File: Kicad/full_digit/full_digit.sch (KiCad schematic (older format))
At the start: 40 parts, among them J1 CONN_8, J2 CONN_8, J3 CONN_8, J4 CONN_8, J5 CONN_8, J6 CONN_8, J7 CONN_8, J8 CONN_8, U1 TLC5917, X1 MTHOLE, X2 MTHOLE, X3 MTHOLE, X4 MTHOLE

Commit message: Added new connectors to schematics
Added DNS connectors for Spark Core/Photon/Electron, Arduino
Uno/Micro/Nano. Also redacted access token for the Spark Core used for
the prototype clock. That Spark has been destroyed, so don't bother
trying to use the token.
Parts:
- removed PTC1, PTC2: 0ZCF0300AF2C, ~, symbol PTC
- added J10, J9: CONN_01X03, symbol CONN_01X03
- added J11, J12: CONN_01X12, symbol CONN_01X12
- added J13, J16: CONN_01X08, symbol CONN_01X08
- added J14: CONN_01X06, symbol CONN_01X06
- added J15: CONN_01X10, symbol CONN_01X10
- added J17, J18: CONN_01X17, symbol CONN_01X17
- added J19: RASM722X, symbol BARREL_JACK
- C2: value 4.7uF 25V -> 4.7uF 50V
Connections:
- net labels added: +5V, Vled
- net labels removed: VLED
- wire segments 81 -> 137
- no-connect marks 0 -> 59
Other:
- note added: "Arduino Micro/Nano Pro"
- note added: "Arduino Uno"
- note added: "Power Input"
- note added: "Regulator"
- note added: "Spark"
- note added: "Vled must be less than 20 V. \nVcc can be between 3.0 and 5.5 V. \nComms should match Vcc."
- note removed: "Vcc can be between 3.0 and 5.5 V. \nComms should match Vcc."
- moved on the sheet: C1, C2, D1, D10, D11, D12, D13, D14, D15, D16, D17, D18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

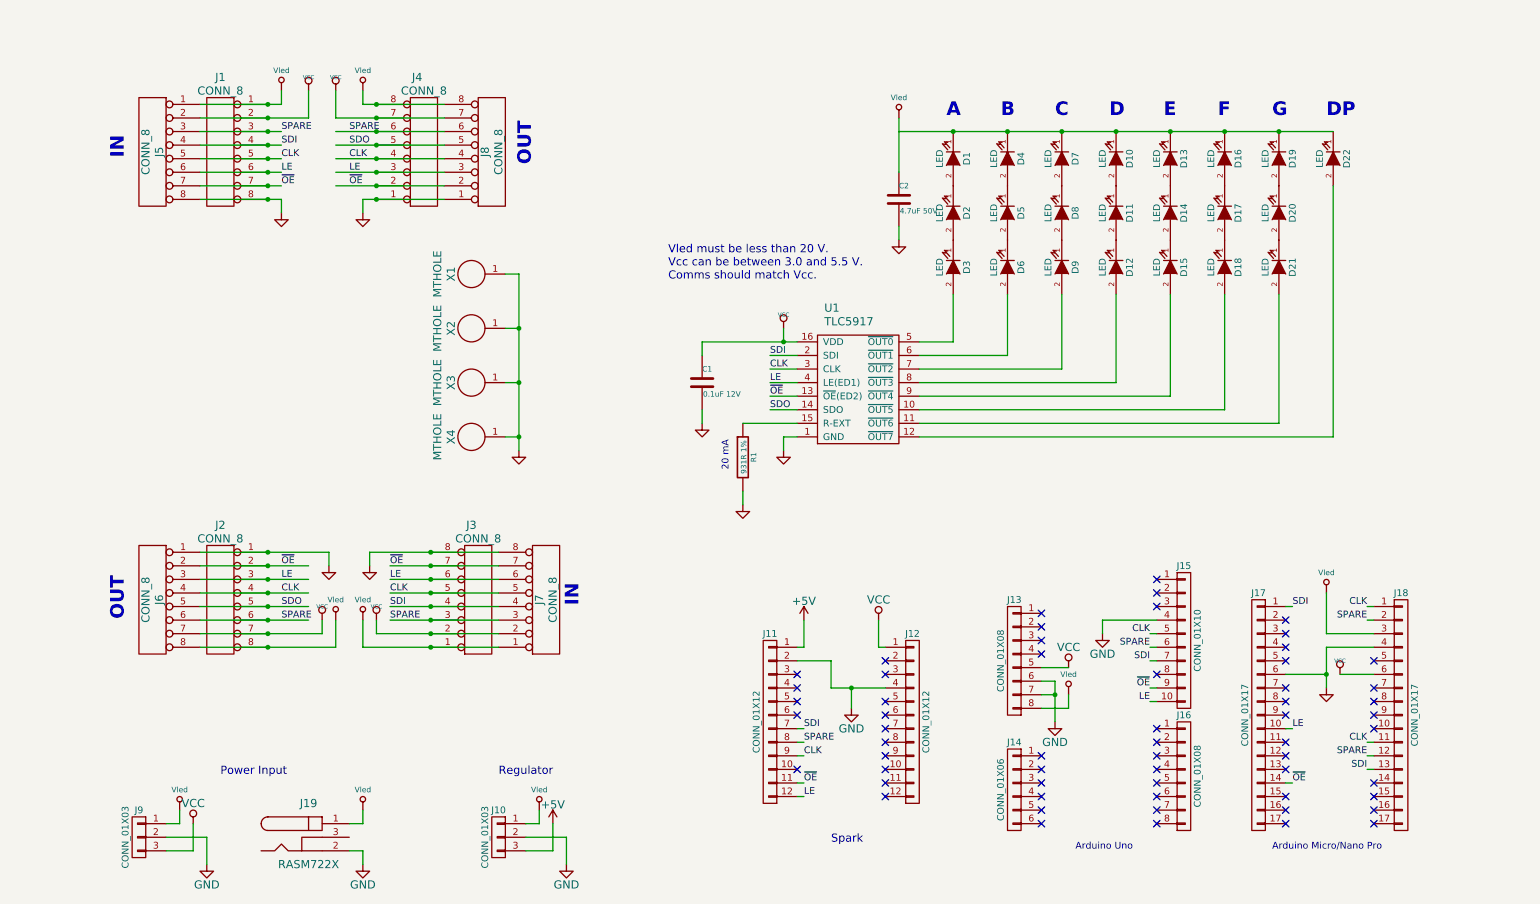
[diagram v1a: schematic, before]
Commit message: Placement of Rev 3
Placed new parts: Spark, Arduino Uno, Arduino Micro, and logo. Routing
still to do.
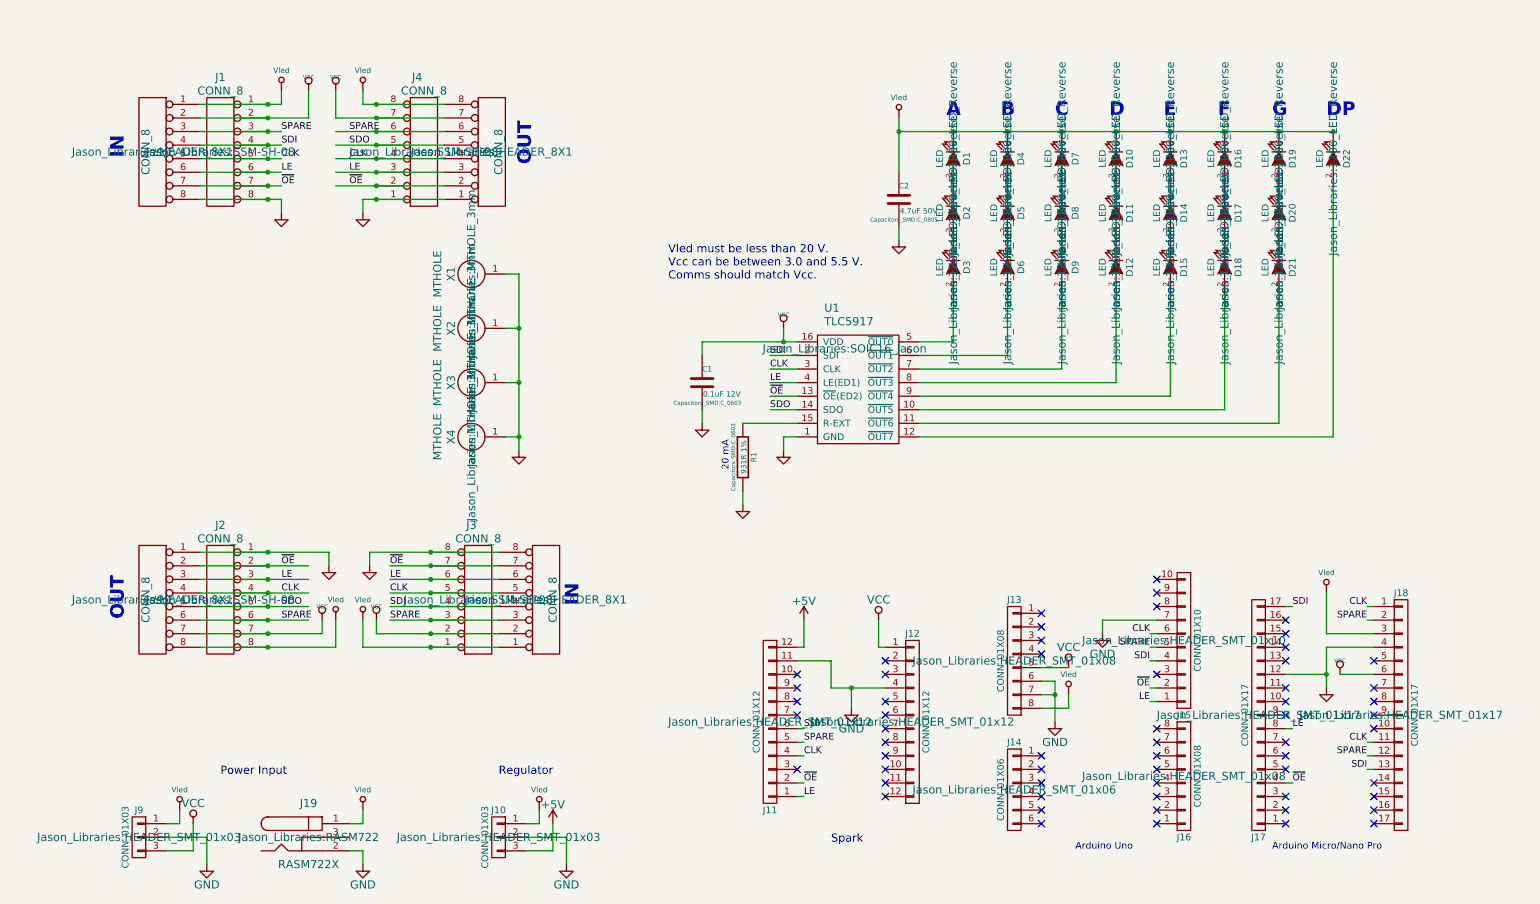
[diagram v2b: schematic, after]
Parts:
- C1, R1: footprint ~ -> Capacitors_SMD:C_0603
- C2: footprint ~ -> Capacitors_SMD:C_0805
- D1, D10, D11, D12, D13, D14, D15, D16, D17, D18, D19, D2, D20, D21, D22, D3, D4, D5, D6, D7, D8, D9: footprint ~ -> Jason_Libraries:1206_LED_Reverse
- J1, J2, J3, J4: footprint (none) -> Jason_Libraries:SSM-SH-08
- J10, J9: footprint (none) -> Jason_Libraries:HEADER_SMT_01x03
- J11, J12: footprint (none) -> Jason_Libraries:HEADER_SMT_01x12
- J13, J16: footprint (none) -> Jason_Libraries:HEADER_SMT_01x08
- J14: footprint (none) -> Jason_Libraries:HEADER_SMT_01x06
- J15: footprint (none) -> Jason_Libraries:HEADER_SMT_01x10
- J17, J18: footprint (none) -> Jason_Libraries:HEADER_SMT_01x17
- J19: footprint (none) -> Jason_Libraries:RASM722
- J5, J6, J7, J8: footprint (none) -> Jason_Libraries:HEADER_8X1
- U1: footprint (none) -> Jason_Libraries:SOIC16_Jason
- X1, X2, X3, X4: footprint (none) -> Jason_Libraries:MTHOLE_3mm

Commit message: Rev 3 Final Draft
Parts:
- J11, J12: footprint Jason_Libraries:HEADER_SMT_01x12 -> Jason_Libraries:HEADER_SMT_01x12_SV
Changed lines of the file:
@@
 F 0 "J12" H 6650 6350 50  0000 C CNN
 F 1 "CONN_01X12" V 6750 5700 50  0000 C CNN
-F 2 "Jason_Libraries:HEADER_SMT_01x12" H 6650 5700 60  0000 C CNN
+F 2 "Jason_Libraries:HEADER_SMT_01x12_SV" H 6650 5700 60  0000 C CNN
 F 3 "" H 6650 5700 60  0000 C CNN
 	1    6650 5700
@@
 F 0 "J11" H 5600 6350 50  0000 C CNN
 F 1 "CONN_01X12" V 5700 5700 50  0000 C CNN
-F 2 "Jason_Libraries:HEADER_SMT_01x12" H 5600 5700 60  0000 C CNN
+F 2 "Jason_Libraries:HEADER_SMT_01x12_SV" H 5600 5700 60  0000 C CNN
 F 3 "" H 5600 5700 60  0000 C CNN
 	1    5600 5700

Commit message: First Rev 4 fixes
* Added NPTH for barrel connector as per issue #21
* Connected shunt and sleeve together to increase chances of capability
with barrel connectors as per issue #20
* Lengthen Arduino pads and double-checked spacing as per issue #19
* Fixed spacing for Spark Cores as per issue #18
* Updated C2 to 1206 as per issue #17
* Fixed LED library to match rotation to IPC spec as per issue #15
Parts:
- C1: symbol C -> C-RESCUE-full_digit
- C2: footprint Capacitors_SMD:C_0805 -> Capacitors_SMD:C_1206_HandSoldering; symbol C -> C-RESCUE-full_digit
- R1: symbol R -> R-RESCUE-full_digit
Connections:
- wire segments 137 -> 138
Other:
- note added: "Iled = 15 * 1.25 V / Rext\nFor 931R, Iled = 20 mA\nSee page 18 of datasheet."
- note removed: "20 mA"
